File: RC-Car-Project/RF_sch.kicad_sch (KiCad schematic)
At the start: 13 parts, among them U1 AT86RF215-ZU, U5 RFX2401C, U6 2450FB15A050E

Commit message: Fixed Annotations
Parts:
- C31: renamed from C24; footprint Capacitor_SMD:C_0201_0603Metric -> Capacitor_SMD:C_0603_1608Metric
- C32: renamed from C25; footprint Capacitor_SMD:C_0201_0603Metric -> Capacitor_SMD:C_0603_1608Metric
- C33: renamed from C26; footprint Capacitor_SMD:C_0201_0603Metric -> Capacitor_SMD:C_0603_1608Metric
- C34: renamed from C27; footprint Capacitor_SMD:C_0201_0603Metric -> Capacitor_SMD:C_0603_1608Metric
- C35: renamed from C28; footprint Capacitor_SMD:C_0201_0603Metric -> Capacitor_SMD:C_0603_1608Metric
- C36: renamed from C29; footprint Capacitor_SMD:C_0201_0603Metric -> Capacitor_SMD:C_0603_1608Metric
- C37: renamed from C30; footprint Capacitor_SMD:C_0201_0603Metric -> Capacitor_SMD:C_0603_1608Metric
- C38: renamed from C31; footprint Capacitor_SMD:C_0201_0603Metric -> Capacitor_SMD:C_0603_1608Metric
- C39: renamed from C32; footprint Capacitor_SMD:C_0201_0603Metric -> Capacitor_SMD:C_0603_1608Metric
- C40: renamed from C33; footprint Capacitor_SMD:C_0201_0603Metric -> Capacitor_SMD:C_0603_1608Metric
- renumbered U1 to U4, U6 to U5, U5 to U6

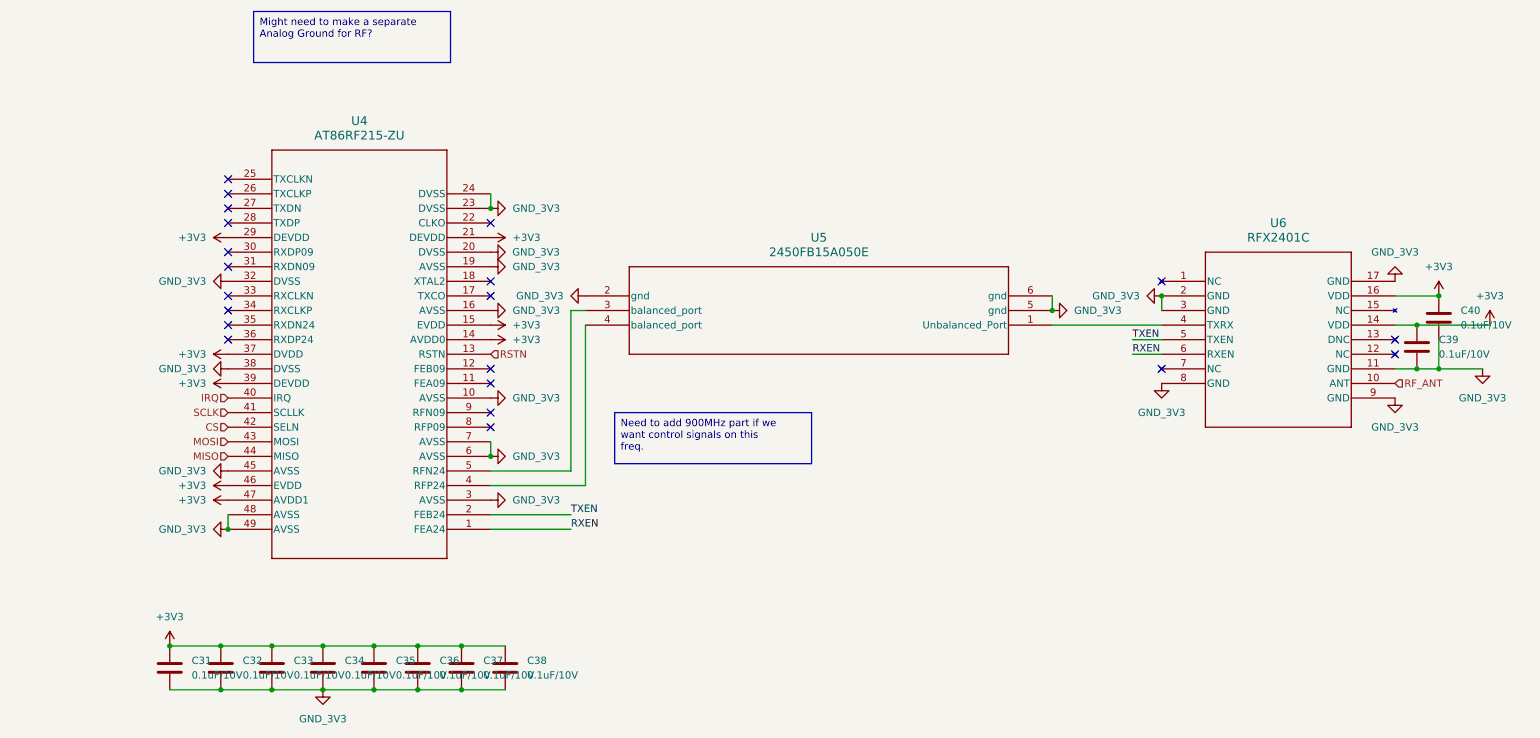
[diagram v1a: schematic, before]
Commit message: Add RF filter + another thermo header + layout everything
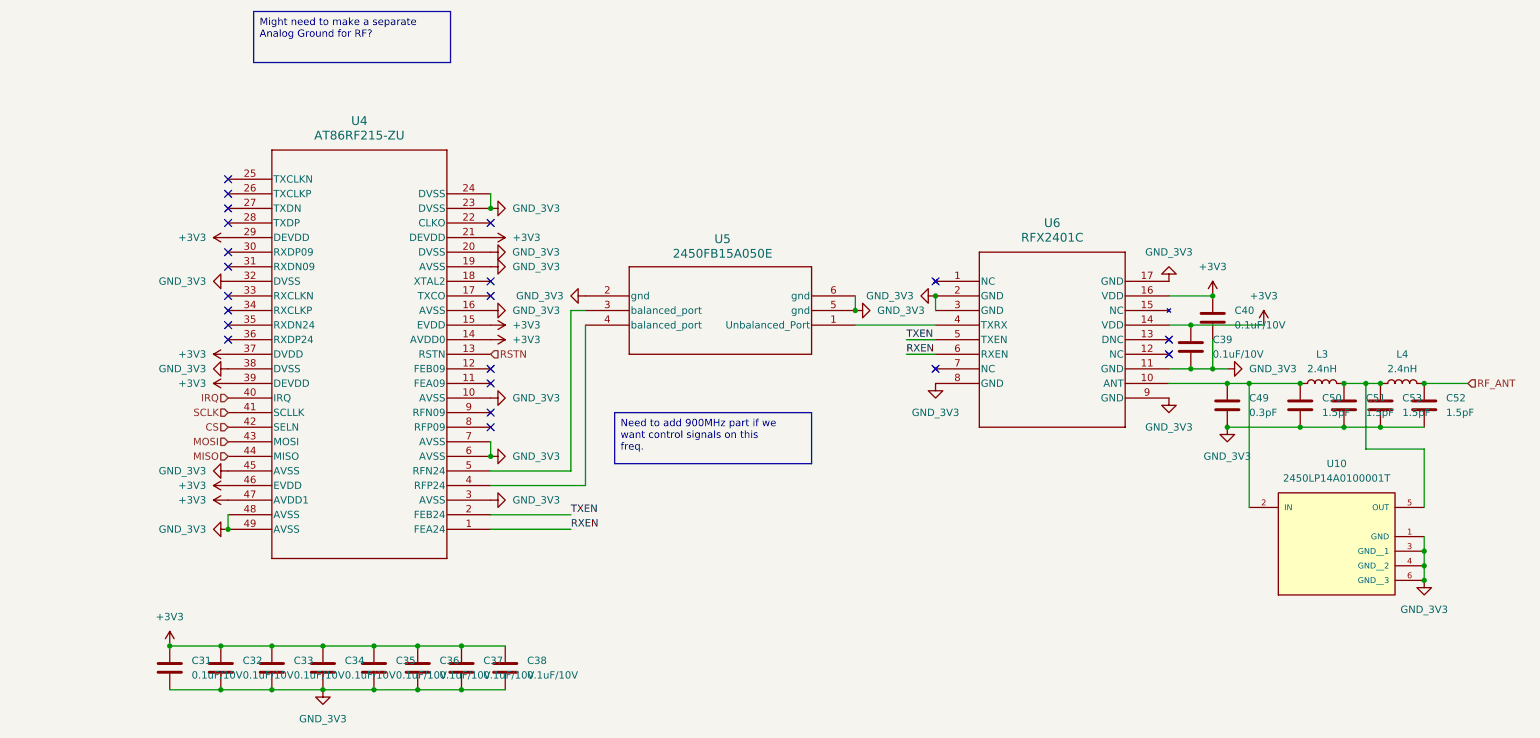
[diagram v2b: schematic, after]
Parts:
- added C49: 0.3pF, Capacitor_SMD:C_0603_1608Metric, symbol Device:C
- added C50, C51, C52, C53: 1.5pF, Capacitor_SMD:C_0603_1608Metric, symbol Device:C
- added L3, L4: 2.4nH, Inductor_SMD:L_0603_1608Metric, symbol Device:L
- added U10: 2450LP14A0100001T, footprints:ICCAF50P160X80X70-6N, symbol 2450LP14A0100001T:2450LP14A0100001T
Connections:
- net GND_3V3: now also C49.2, C50.2, C51.2, C52.2, C53.2, U10.1 (GND), U10.3 (GND__1), U10.4 (GND__2), U10.6 (GND__3)
- net RF_ANT: now also C52.1, L4.2; no longer U6.10 (ANT)
- new net: C49.1, C50.1, L3.1, U10.2 (IN), U6.10 (ANT)
- new net: C51.1, C53.1, L3.2, L4.1, U10.5 (OUT)
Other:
- moved on the sheet: C39, C40, U5, U6

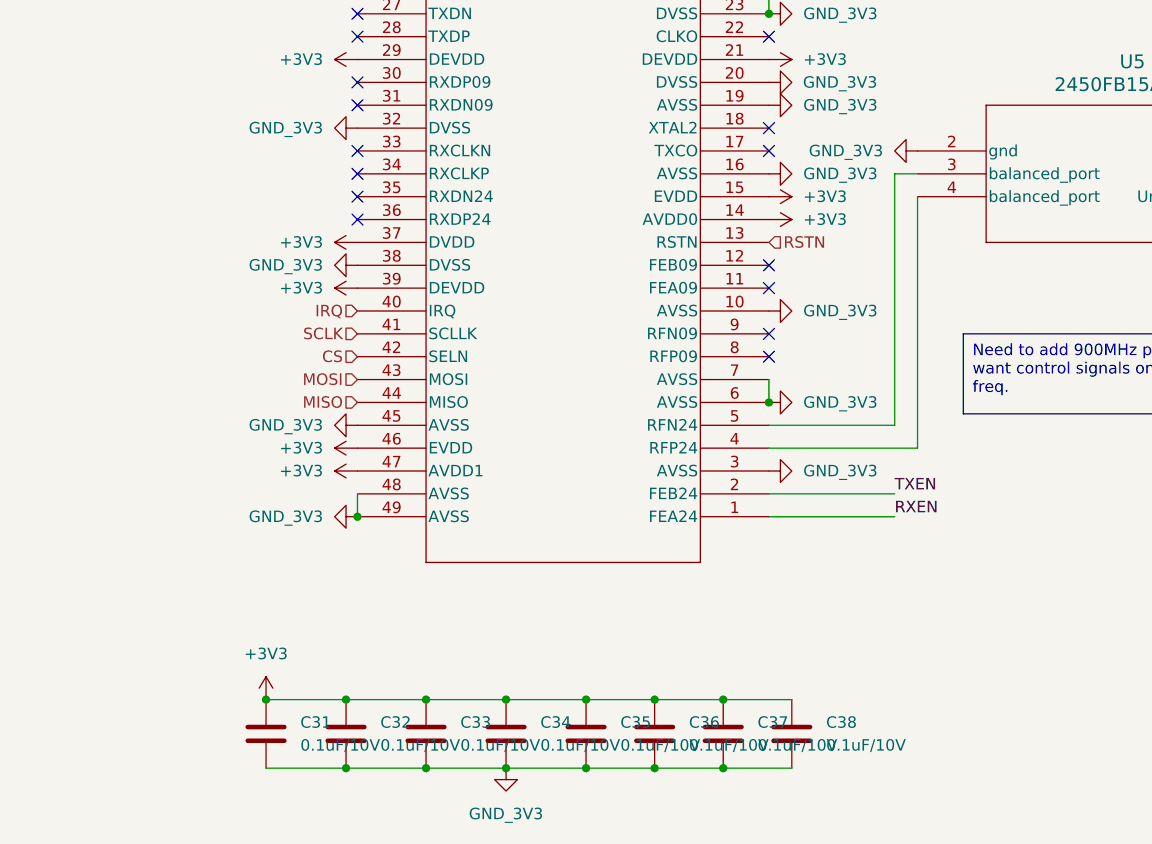
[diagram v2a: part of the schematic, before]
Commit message: fix at86 power connections
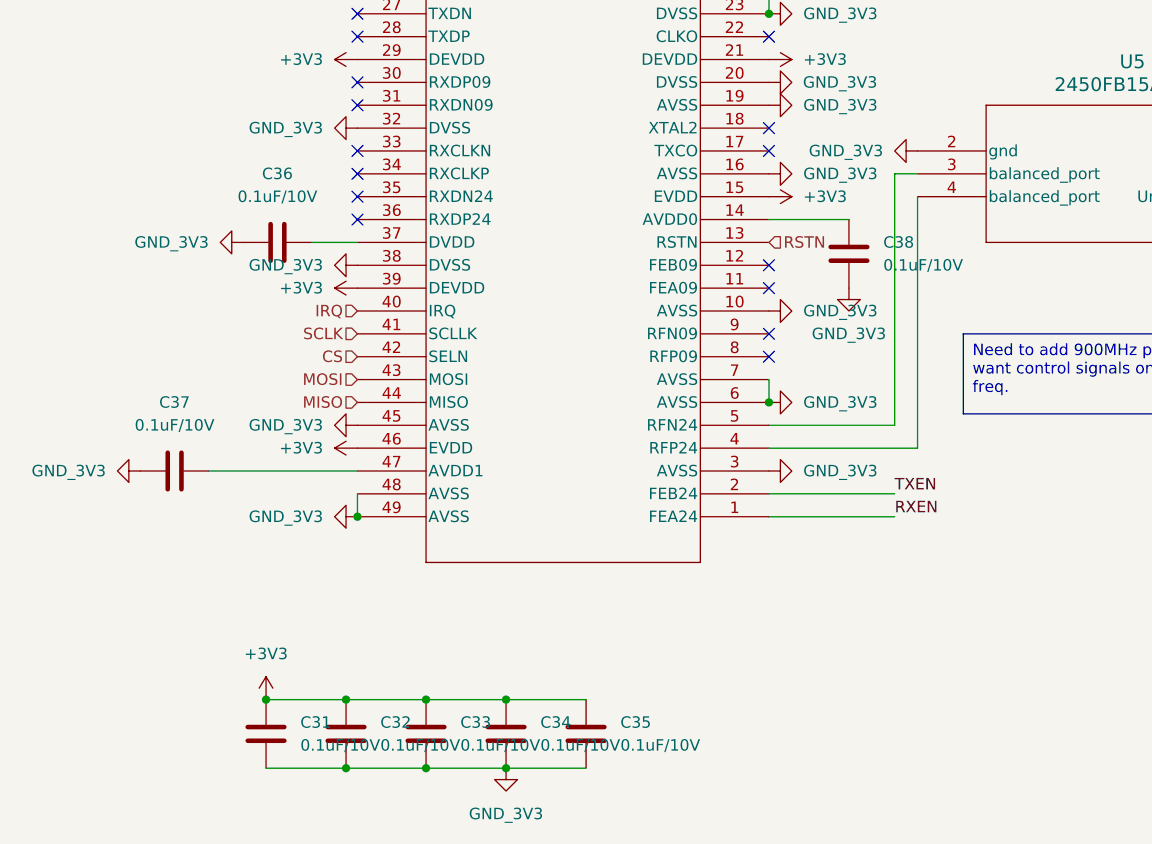
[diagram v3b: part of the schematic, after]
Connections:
- net +3V3: no longer C36.1, C37.1, C38.1, U4.14 (AVDD0), U4.37 (DVDD), U4.47 (AVDD1)
- net GND_3V3: now also C36.1, C37.1; no longer C36.2, C37.2
- new net: C38.1, U4.14 (AVDD0)
- new net: C36.2, U4.37 (DVDD)
- new net: C37.2, U4.47 (AVDD1)
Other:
- moved on the sheet: C36, C37, C38

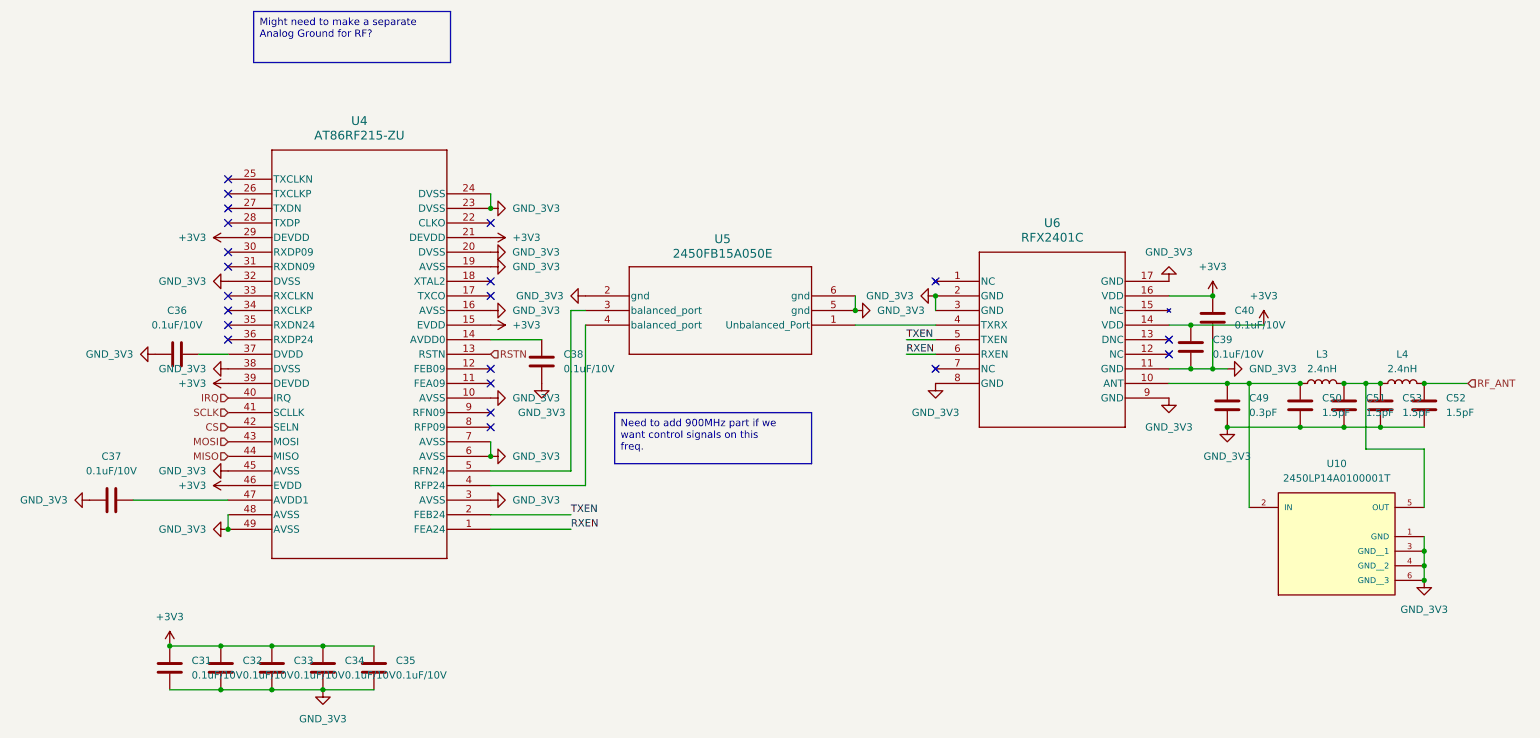
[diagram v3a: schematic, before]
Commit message: Added functionality to the STM32 on the tank PCB
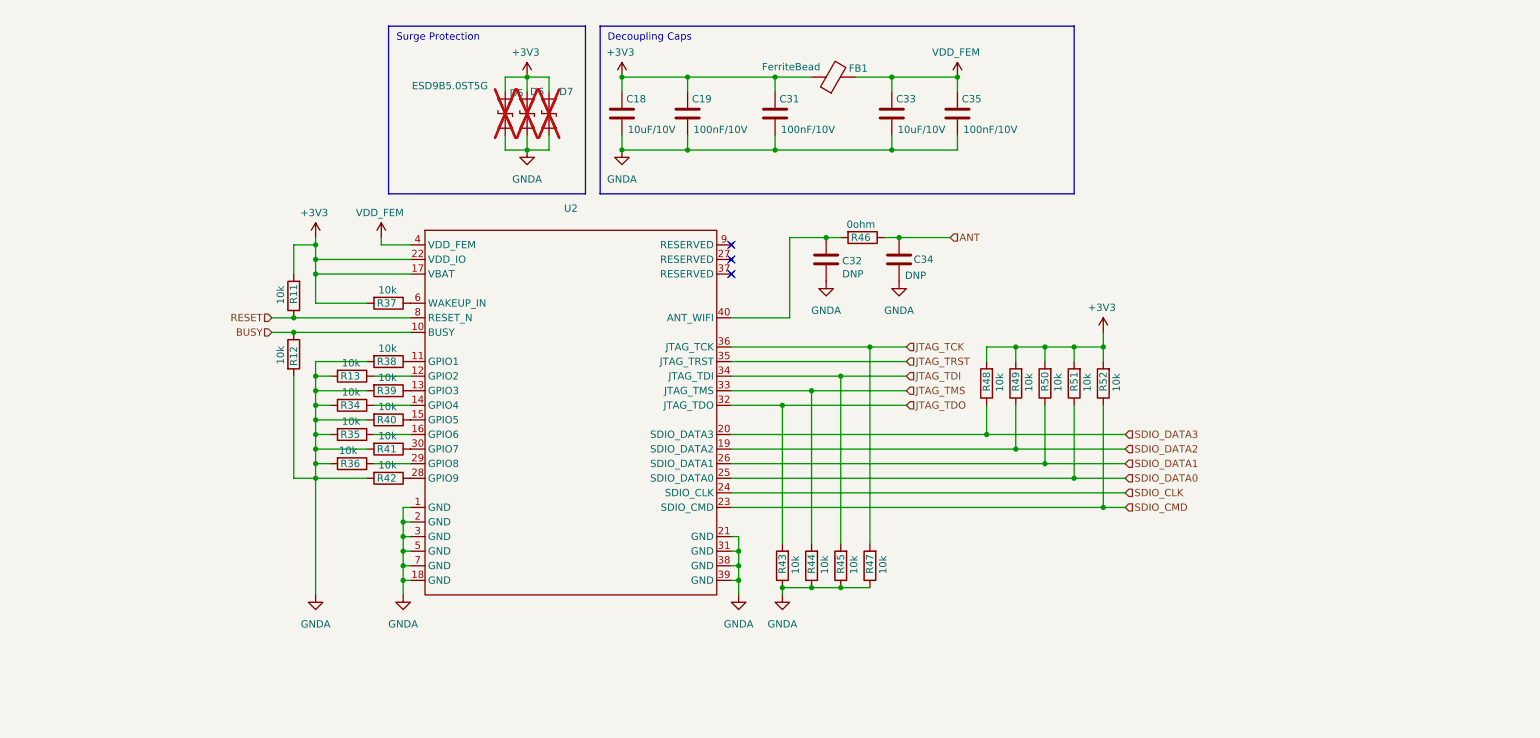
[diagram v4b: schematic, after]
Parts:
- removed C36, C37, C38, C39, C40: 0.1uF/10V, Capacitor_SMD:C_0603_1608Metric, symbol Device:C
- removed C49: 0.3pF, Capacitor_SMD:C_0603_1608Metric, symbol Device:C
- removed C50, C51, C52, C53: 1.5pF, Capacitor_SMD:C_0603_1608Metric, symbol Device:C
- removed L3, L4: 2.4nH, Inductor_SMD:L_0603_1608Metric, symbol Device:L
- removed U10: 2450LP14A0100001T, footprints:ICCAF50P160X80X70-6N, symbol 2450LP14A0100001T:2450LP14A0100001T
- removed U4: AT86RF215-ZU, footprints:QFN48_PQ_MCH, symbol AT86RF215:AT86RF215-ZU
- removed U5: 2450FB15A050E, footprints:2450FB15A050E_JOT, symbol 2450FB15A050E Balun:2450FB15A050E
- removed U6: RFX2401C, footprints:RFX2401C_SKY, symbol RFX2401C:RFX2401C
- added C18: 10uF/10V, Capacitor_SMD:C_0603_1608Metric, symbol Device:C
- added C19: 100nF/10V, Capacitor_SMD:C_0603_1608Metric, symbol Device:C
- added D5, D6, D7: ESD9B5.0ST5G, Diode_SMD:D_SOD-923, symbol Diode:ESD9B5.0ST5G
- added FB1: FerriteBead, Capacitor_SMD:C_0603_1608Metric, symbol Device:FerriteBead
- added R11, R12, R13, R34, R35, R36, R37, R38, R39, R40, R41, R42, R43, R44, R45, R47, R48, R49, R50, R51, R52: 10k, Capacitor_SMD:C_0603_1608Metric, symbol Device:R
- added R46: 0ohm, Resistor_SMD:R_0603_1608Metric, symbol Device:R
- added U2: ~, FGH100M:FGH100MABMD, symbol FGH100M:FGH100MABMD
- C31, C35: value 0.1uF/10V -> 100nF/10V
- C32, C34: value 0.1uF/10V -> DNP
- C33: value 0.1uF/10V -> 10uF/10V
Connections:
- net +3V3: now also C18.1, C19.1, D5.2 (A2), D6.2 (A2), D7.2 (A2), FB1.1, R11.2, R37.2, R48.2, R49.2, R50.2, R51.2, R52.2, U2.17 (VBAT), U2.22 (VDD_IO); no longer C32.1, C33.1, C34.1, C35.1
- net GND_3V3 renamed GNDA
- net GNDA: now also C18.2, C19.2, D5.1 (A1), D6.1 (A1), D7.1 (A1), R12.2, R13.2, R34.2, R35.2, R36.2, R38.2, R39.2, R40.2, R41.2, R42.2, R43.1, R44.1, R45.1, R47.1, U2.1 (GND), U2.18 (GND), U2.2 (GND), U2.21 (GND), U2.3 (GND), U2.31 (GND), U2.38 (GND), U2.39 (GND), U2.5 (GND), U2.7 (GND)
- new net: R35.1, U2.16 (GPIO6)
- new net: R13.1, U2.12 (GPIO2)
- new net: R38.1, U2.11 (GPIO1)
- new net: R39.1, U2.13 (GPIO3)
- new net: R34.1, U2.14 (GPIO4)
- new net: R40.1, U2.15 (GPIO5)
- new net: R42.1, U2.28 (GPIO9)
- new net: R36.1, U2.29 (GPIO8)
- new net: R41.1, U2.30 (GPIO7)
- new net: C32.1, R46.2, U2.40 (ANT_WIFI)
- new net: R37.1, U2.6 (WAKEUP_IN)
- new net ANT: C34.1, R46.1
- new net BUSY: R12.1, U2.10 (BUSY)
- new net JTAG_TCK: R47.2, U2.36 (JTAG_TCK)
- new net JTAG_TDI: R45.2, U2.34 (JTAG_TDI)
- new net JTAG_TDO: R43.2, U2.32 (JTAG_TDO)
- new net JTAG_TMS: R44.2, U2.33 (JTAG_TMS)
- new net JTAG_TRST: U2.35 (JTAG_TRST)
- new net RESET: R11.1, U2.8 (RESET_N)
- new net SDIO_CLK: U2.24 (SDIO_CLK)
- new net SDIO_CMD: R52.1, U2.23 (SDIO_CMD)
- new net SDIO_DATA0: R51.1, U2.25 (SDIO_DATA0)
- new net SDIO_DATA1: R50.1, U2.26 (SDIO_DATA1)
- new net SDIO_DATA2: R49.1, U2.19 (SDIO_DATA2)
- new net SDIO_DATA3: R48.1, U2.20 (SDIO_DATA3)
- new net VDD_FEM: C33.1, C35.1, FB1.2, U2.4 (VDD_FEM)
- no-connect marks 21 -> 3
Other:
- note added: "Decoupling Caps"
- note added: "Surge Protection"

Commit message: Fixed Resistors
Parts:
- added R63: 10k, Capacitor_SMD:C_0603_1608Metric, symbol Device:R
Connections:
- net +3V3: now also R63.2
- net SDIO_CLK: now also R63.1
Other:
- moved on the sheet: R48, R49, R50, R51, R52

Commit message: Re added my fuse
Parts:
- FB1: MANUF_PN (none) -> HCB 1608KF-181T20
- U2: MANUF_PN (none) -> FGH100MABMD
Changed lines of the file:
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@@
 			)
 		)
-		(property "MANUF_PN" ""
+		(property "MANUF_PN" "FGH100MABMD"
 			(at 119.38 109.22 0)
 			(effects
@@
 			)
 		)
-		(property "MANUF_PN" ""
+		(property "MANUF_PN" "HCB 1608KF-181T20"
 			(at 165.1 49.53 0)
 			(effects

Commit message: Resistor manuf PNs labelled
resistor manufacturer part numbers added
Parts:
- R11, R12, R13, R34, R35, R36, R37, R38, R39, R40, R41, R42, R43, R44, R45, R47, R48, R49, R50, R51, R52, R63: MANUF_PN (none) -> RC0603FR-0710KL
- R46: MANUF_PN (none) -> RMCF0603ZT0R00
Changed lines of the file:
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@@
 			)
 		)
-		(property "MANUF_PN" ""
+		(property "MANUF_PN" "RC0603FR-0710KL"
 			(at 199.39 102.87 0)
 			(effects
@@
 			)
 		)
-		(property "MANUF_PN" ""
+		(property "MANUF_PN" "RC0603FR-0710KL"
 			(at 81.28 111.76 0)
 			(effects
@@
 			)
 		)
-		(property "MANUF_PN" ""
+		(property "MANUF_PN" "RC0603FR-0710KL"
 			(at 71.12 87.63 0)
 			(effects
@@
 			)
 		)
-		(property "MANUF_PN" ""
+		(property "MANUF_PN" "RC0603FR-0710KL"
 			(at 81.28 101.6 0)
 			(effects
@@
 			)
 		)
-		(property "MANUF_PN" ""
+		(property "MANUF_PN" "RC0603FR-0710KL"
 			(at 204.47 102.87 0)
 			(effects
@@
 			)
 		)
-		(property "MANUF_PN" ""
+		(property "MANUF_PN" "RC0603FR-0710KL"
 			(at 171.45 134.62 0)
 			(effects
@@
 			)
 		)
-		(property "MANUF_PN" ""
+		(property "MANUF_PN" "RC0603FR-0710KL"
 			(at 87.63 88.9 0)
 			(effects
@@
 			)
 		)
-		(property "MANUF_PN" ""
+		(property "MANUF_PN" "RC0603FR-0710KL"
 			(at 209.55 102.87 0)
 			(effects
@@
 			)
 		)
-		(property "MANUF_PN" ""
+		(property "MANUF_PN" "RC0603FR-0710KL"
 			(at 189.23 102.87 0)
 			(effects
@@
 			)
 		)
-		(property "MANUF_PN" ""
+		(property "MANUF_PN" "RC0603FR-0710KL"
 			(at 81.28 116.84 0)
 			(effects
@@
 			)
 		)
-		(property "MANUF_PN" ""
+		(property "MANUF_PN" "RC0603FR-0710KL"
 			(at 87.63 99.06 0)
 			(effects
@@
 			)
 		)
-		(property "MANUF_PN" ""
+		(property "MANUF_PN" "RC0603FR-0710KL"
 			(at 194.31 102.87 0)
 			(effects
@@
 			)
 		)
-		(property "MANUF_PN" ""
+		(property "MANUF_PN" "RMCF0603ZT0R00"
 			(at 170.18 77.47 0)
 			(effects
@@
 			)
 		)
-		(property "MANUF_PN" ""
+		(property "MANUF_PN" "RC0603FR-0710KL"
 			(at 87.63 104.14 0)
 			(effects
@@
 			)
 		)
-		(property "MANUF_PN" ""
+		(property "MANUF_PN" "RC0603FR-0710KL"
 			(at 214.63 102.87 0)
 			(effects
@@
 			)
 		)
-		(property "MANUF_PN" ""
+		(property "MANUF_PN" "RC0603FR-0710KL"
 			(at 87.63 109.22 0)
 			(effects
@@
 			)
 		)
-		(property "MANUF_PN" ""
+		(property "MANUF_PN" "RC0603FR-0710KL"
 			(at 87.63 119.38 0)
 			(effects
@@
 			)
 		)
-		(property "MANUF_PN" ""
+		(property "MANUF_PN" "RC0603FR-0710KL"
 			(at 87.63 114.3 0)
 			(effects
@@
 			)
 		)
-		(property "MANUF_PN" ""
+		(property "MANUF_PN" "RC0603FR-0710KL"
 			(at 156.21 134.62 0)
 			(effects
@@
 			)
 		)
-		(property "MANUF_PN" ""
+		(property "MANUF_PN" "RC0603FR-0710KL"
 			(at 71.12 97.79 0)
 			(effects
@@
 			)
 		)
-		(property "MANUF_PN" ""
+		(property "MANUF_PN" "RC0603FR-0710KL"
 			(at 161.29 134.62 0)
 			(effects
@@
 			)
 		)
-		(property "MANUF_PN" ""
+		(property "MANUF_PN" "RC0603FR-0710KL"
 			(at 166.37 134.62 0)
 			(effects
@@
 			)
 		)
-		(property "MANUF_PN" ""
+		(property "MANUF_PN" "RC0603FR-0710KL"
 			(at 81.28 106.68 0)
 			(effects
